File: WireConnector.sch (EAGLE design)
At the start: 2 parts

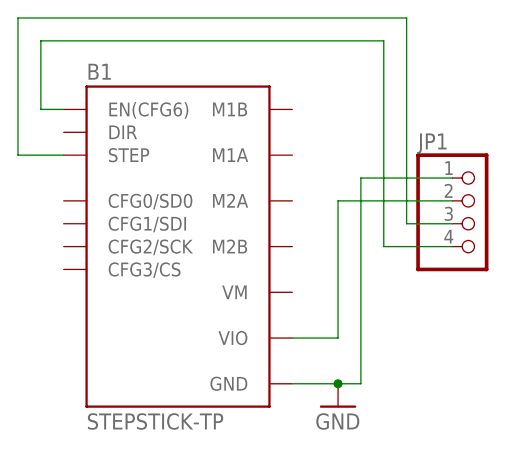
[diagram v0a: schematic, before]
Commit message: Changed PWR connection position 2 Layer design GND Plate both sites Naming completed
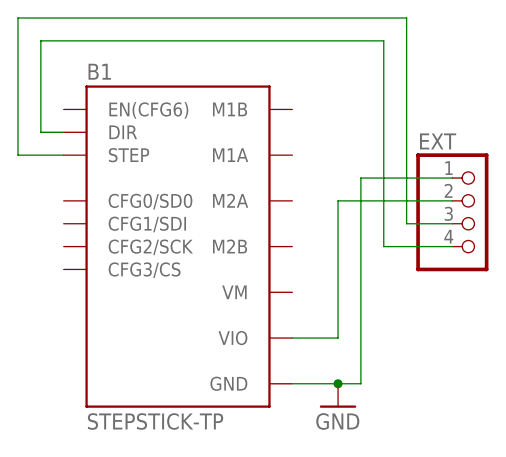
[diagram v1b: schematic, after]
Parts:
- renumbered JP1 to EXT
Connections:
- net N$4: now also B1.DIR; no longer B1.EN(CFG6)
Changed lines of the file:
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@@
 <?xml version="1.0" encoding="utf-8"?>
 <!DOCTYPE eagle SYSTEM "eagle.dtd">
-<eagle version="7.2.0">
+<eagle version="7.7.0">
 <drawing>
 <settings>
@@
 <parts>
 <part name="B1" library="we-board" deviceset="STEPSTICK" device="-TP"/>
-<part name="JP1" library="pinhead" deviceset="PINHD-1X4" device=""/>
+<part name="EXT" library="pinhead" deviceset="PINHD-1X4" device=""/>
 <part name="GND1" library="supply1" deviceset="GND" device=""/>
 </parts>
@@
 <instances>
 <instance part="B1" gate="BOARD" x="68.58" y="60.96"/>
-<instance part="JP1" gate="A" x="101.6" y="63.5"/>
+<instance part="EXT" gate="A" x="101.6" y="63.5"/>
 <instance part="GND1" gate="1" x="86.36" y="43.18"/>
 </instances>
@@
 <net name="N$2" class="2">
 <segment>
-<pinref part="JP1" gate="A" pin="2"/>
+<pinref part="EXT" gate="A" pin="2"/>
 <wire x1="99.06" y1="66.04" x2="86.36" y2="66.04" width="0.1524" layer="91"/>
 <wire x1="86.36" y1="66.04" x2="86.36" y2="50.8" width="0.1524" layer="91"/>
@@
 <net name="N$3" class="1">
 <segment>
-<pinref part="JP1" gate="A" pin="3"/>
+<pinref part="EXT" gate="A" pin="3"/>
 <wire x1="99.06" y1="63.5" x2="93.98" y2="63.5" width="0.1524" layer="91"/>
 <wire x1="93.98" y1="63.5" x2="93.98" y2="86.36" width="0.1524" layer="91"/>
@@
 <net name="N$4" class="2">
 <segment>
-<pinref part="JP1" gate="A" pin="4"/>
+<pinref part="EXT" gate="A" pin="4"/>
 <wire x1="99.06" y1="60.96" x2="91.44" y2="60.96" width="0.1524" layer="91"/>
 <wire x1="91.44" y1="60.96" x2="91.44" y2="83.82" width="0.1524" layer="91"/>
 <wire x1="91.44" y1="83.82" x2="53.34" y2="83.82" width="0.1524" layer="91"/>
-<wire x1="53.34" y1="83.82" x2="53.34" y2="76.2" width="0.1524" layer="91"/>
-<pinref part="B1" gate="BOARD" pin="EN(CFG6)"/>
-<wire x1="53.34" y1="76.2" x2="55.88" y2="76.2" width="0.1524" layer="91"/>
+<wire x1="53.34" y1="83.82" x2="53.34" y2="73.66" width="0.1524" layer="91"/>
+<pinref part="B1" gate="BOARD" pin="DIR"/>
+<wire x1="55.88" y1="73.66" x2="53.34" y2="73.66" width="0.1524" layer="91"/>
 </segment>
 </net>
 <net name="GND" class="2">
 <segment>
-<pinref part="JP1" gate="A" pin="1"/>
+<pinref part="EXT" gate="A" pin="1"/>
 <wire x1="99.06" y1="68.58" x2="88.9" y2="68.58" width="0.1524" layer="91"/>
 <wire x1="88.9" y1="68.58" x2="88.9" y2="45.72" width="0.1524" layer="91"/>
